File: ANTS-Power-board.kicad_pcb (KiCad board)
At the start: 2 copper layers, 90 x 90 mm, 6 parts, among them U1 TPS62916RPYR, U2 LP2985-3.3

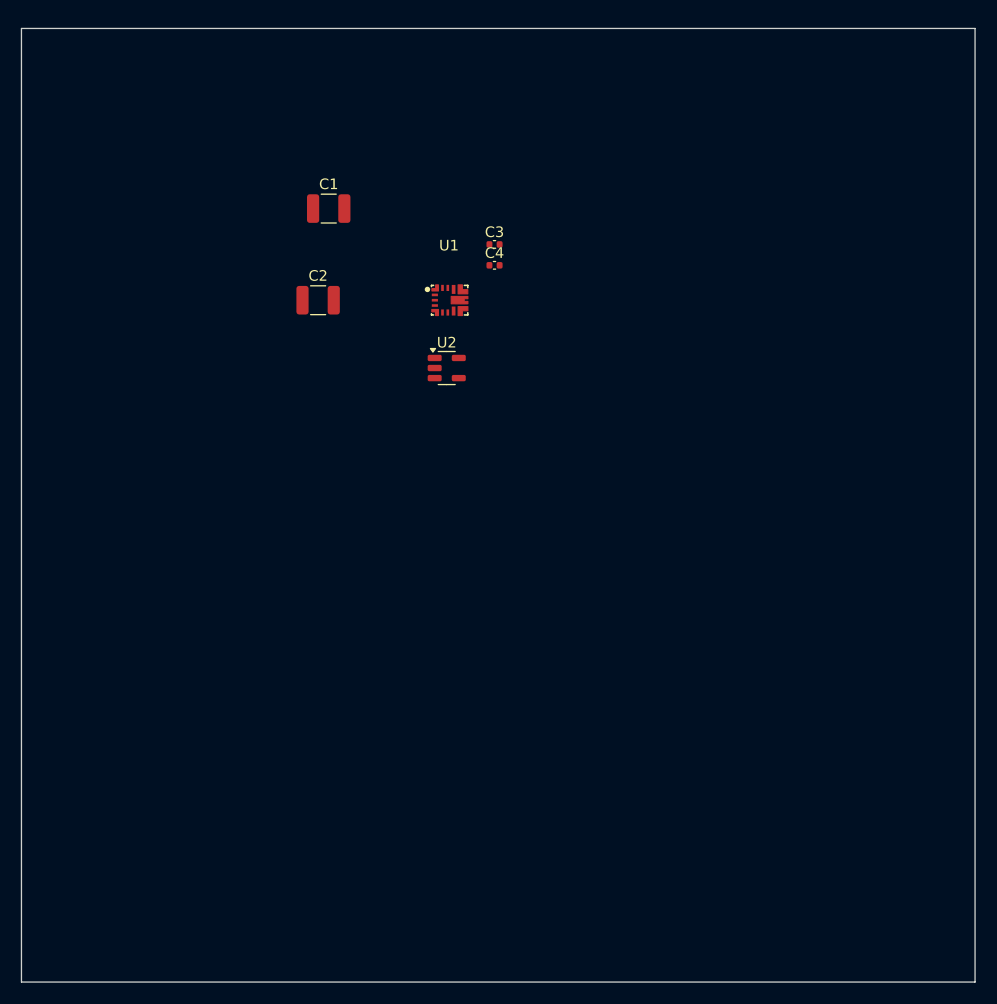
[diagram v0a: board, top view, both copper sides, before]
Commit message: Schematic finished; PCB ready for basic layout
Finished the ferrite bead footprint and setup the schematic for the PCB. Schematic has been portered over to the PCB Editor and is ready to start the basic parts layout. The PCB board is set up for the most part there are still some things to set up, but that's for later.
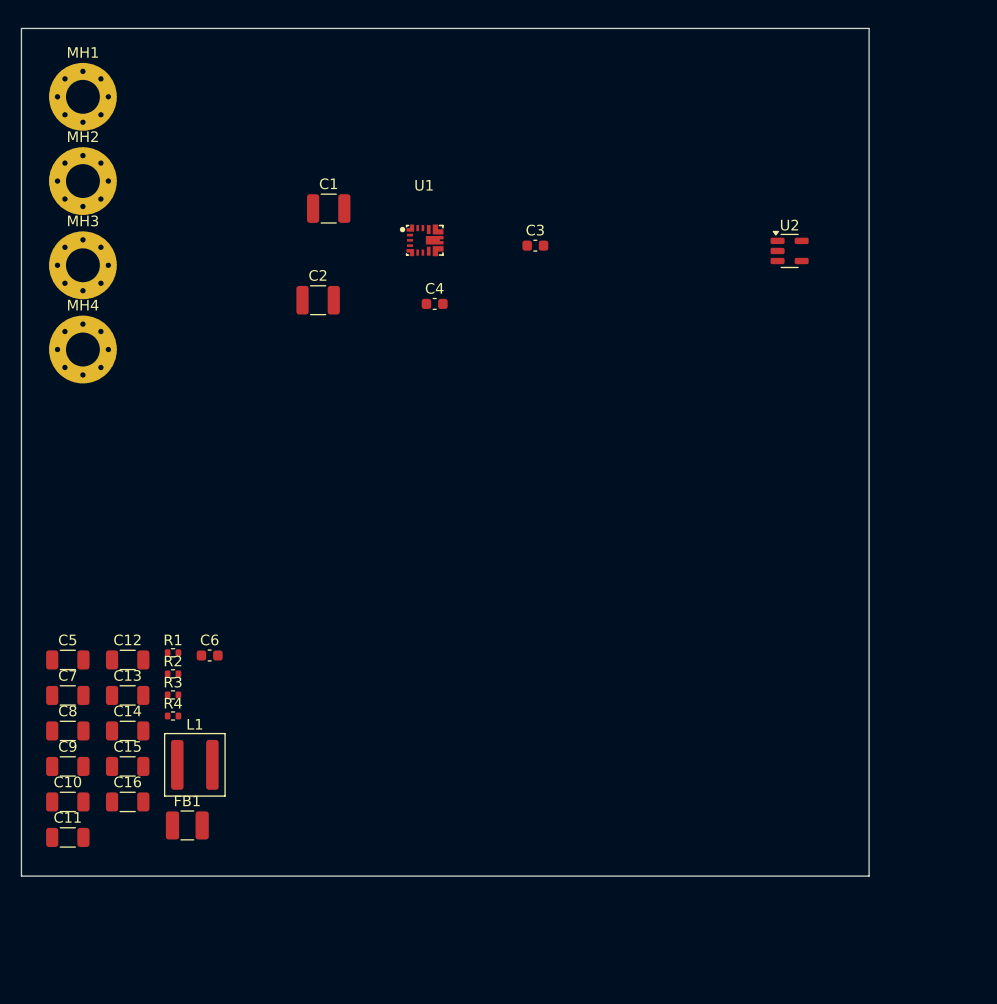
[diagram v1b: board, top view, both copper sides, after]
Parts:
- added C10: 22uF, Capacitor_SMD:C_1206_3216Metric, F.Cu at (104.4, 143.0)
- added C11: 22uF, Capacitor_SMD:C_1206_3216Metric, F.Cu at (104.4, 146.3)
- added C12: 22uF, Capacitor_SMD:C_1206_3216Metric, F.Cu at (110.0, 129.6)
- added C13: 22uF, Capacitor_SMD:C_1206_3216Metric, F.Cu at (110.0, 132.9)
- added C14: 22uF, Capacitor_SMD:C_1206_3216Metric, F.Cu at (110.0, 136.3)
- added C15: 22uF, Capacitor_SMD:C_1206_3216Metric, F.Cu at (110.0, 139.7)
- added C16: 22uF, Capacitor_SMD:C_1206_3216Metric, F.Cu at (110.0, 143.0)
- added C5: 100nF, Capacitor_SMD:C_1206_3216Metric, F.Cu at (104.4, 129.6)
- added C6: 470nF, Capacitor_SMD:C_0603_1608Metric, F.Cu at (117.8, 129.2)
- added C7: 22uF, Capacitor_SMD:C_1206_3216Metric, F.Cu at (104.4, 132.9)
- added C8: 22uF, Capacitor_SMD:C_1206_3216Metric, F.Cu at (104.4, 136.3)
- added C9: 22uF, Capacitor_SMD:C_1206_3216Metric, F.Cu at (104.4, 139.7)
- added FB1: FerriteBead, Inductor_SMD:L_1210_3225Metric, F.Cu at (115.7, 145.2)
- added L1: 1uH, Inductor_SMD:L_Coilcraft_XAL5030-XXX, F.Cu at (116.4, 139.5)
- added MH1: M3, MountingHole:MountingHole_3.2mm_M3_Pad_Via, F.Cu at (105.8, 76.5)
- added MH2: M3, MountingHole:MountingHole_3.2mm_M3_Pad_Via, F.Cu at (105.8, 84.4)
- added MH3: M3, MountingHole:MountingHole_3.2mm_M3_Pad_Via, F.Cu at (105.8, 92.4)
- added MH4: M3, MountingHole:MountingHole_3.2mm_M3_Pad_Via, F.Cu at (105.8, 100.3)
- added R1: 18.2k, Resistor_SMD:R_0402_1005Metric, F.Cu at (114.3, 128.9)
- added R2: 10k, Resistor_SMD:R_0402_1005Metric, F.Cu at (114.3, 130.9)
- added R3: 25.5k, Resistor_SMD:R_0402_1005Metric, F.Cu at (114.3, 132.9)
- added R4: 4.87k, Resistor_SMD:R_0402_1005Metric, F.Cu at (114.3, 134.9)
- C3, C4: footprint Capacitor_SMD:C_0402_1005Metric -> Capacitor_SMD:C_0603_1608Metric
- moved U2 34.2 mm to (172.5, 91.0)
- moved C4 6.72 mm to (139.0, 96.0)
- moved U1 6.12 mm to (138.0, 90.0)
- moved C3 3.85 mm to (148.5, 90.5)
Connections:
- net Net-(C5-Pad1) renamed /5V SMPS/SW
- U1 pad 14: Net-(U1-BOOT) -> /5V SMPS/BOOT
- U1 pad 2: Net-(U1-NR/SS) -> /5V SMPS/NR/SS
- U1 pad 3: Net-(U1-FB) -> /5V SMPS/FB
- U1 pad 4: Net-(U1-VO) -> /5V SMPS/VO
- U1 pad 5: Net-(U1-PG) -> /5V SMPS/PG
- U1 pad 6: Net-(U1-S-CONF) -> /5V SMPS/S-CONF
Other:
- board size 90 x 90 mm -> 80 x 80 mm
- rule pad_to_mask_clearance: 0 -> 0.1

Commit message: Wiring done; grounding and error checking still needs to be done
Wiring done; everything still needs to be grounded, error checking, labeling on the board, and final stuff like that still need to be done
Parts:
- moved MH4 83.1 mm to (175.5, 145.5)
- moved C16 77.3 mm to (166.7, 90.3), turned to 90 degrees
- moved C15 73.2 mm to (164.2, 90.3), turned to 90 degrees
- moved MH2 70.4 mm to (175.5, 74.5)
- moved FB1 68.1 mm to (157.8, 91.8), turned to 180 degrees
- moved C11 64.9 mm to (134.0, 88.6), turned to 90 degrees
- moved U2 60.4 mm to (136.5, 139.5)
- moved C9 57.8 mm to (131.5, 88.6), turned to 90 degrees
- moved C10 54.9 mm to (131.4, 95.2), turned to -90 degrees
- moved MH3 53.2 mm to (104.5, 145.5)
- moved C13 51.7 mm to (136.5, 88.6), turned to 90 degrees
- moved C7 50.7 mm to (129.0, 88.6), turned to 90 degrees
- moved C14 48.9 mm to (136.4, 95.2), turned to -90 degrees
- moved L1 48.1 mm to (122.9, 91.8), turned to 180 degrees
- moved C8 47.9 mm to (128.9, 95.2), turned to -90 degrees
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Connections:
- C10 pad 1: /5V SMPS/VO -> 5V_out
- C11 pad 1: /5V SMPS/VO -> 5V_out
- C12 pad 1: /5V SMPS/VO -> 5V_out
- C13 pad 1: /5V SMPS/VO -> 5V_out
- C14 pad 1: /5V SMPS/VO -> 5V_out
- C7 pad 1: /5V SMPS/VO -> 5V_out
- C8 pad 1: /5V SMPS/VO -> 5V_out
- C9 pad 1: /5V SMPS/VO -> 5V_out
- FB1 pad 2: /5V SMPS/VO -> 5V_out
- L1 pad 1: /5V SMPS/VO -> 5V_out
- R2 pad 1: /5V SMPS/VO -> 5V_out
- R3 pad 1: /5V SMPS/VO -> 5V_out
- U1 pad 4: /5V SMPS/VO -> 5V_out
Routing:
- net 5V_out: track 0.00 -> 192.7 mm
- net VBAT+: track 0.00 -> 32.3 mm
- net /5V SMPS/SW: track 0.00 -> 9.90 mm
- net /5V SMPS/BOOT: track 0.00 -> 5.52 mm
- net /5V SMPS/FB: track 0.00 -> 3.90 mm
- net /5V SMPS/NR/SS: track 0.00 -> 2.65 mm
- net /5V SMPS/PG: track 0.00 -> 1.99 mm
- net /5V SMPS/S-CONF: track 0.00 -> 1.09 mm
- net VBAT-: vias 0 -> 51
- added copper zone on B.Cu, net VBAT-

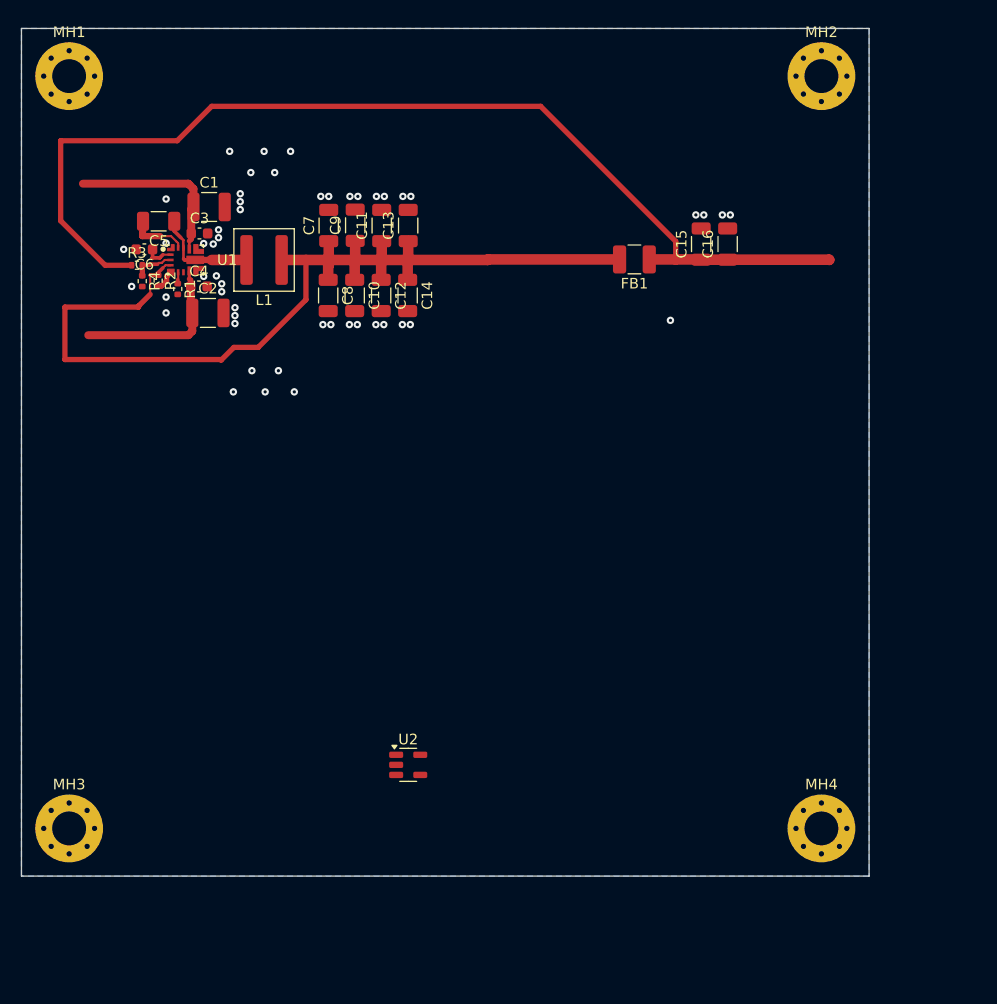
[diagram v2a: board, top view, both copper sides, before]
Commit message: Add connectors & adjust board cuts
- Add DF11 and ScrewTerminals
- Add new edge cuts
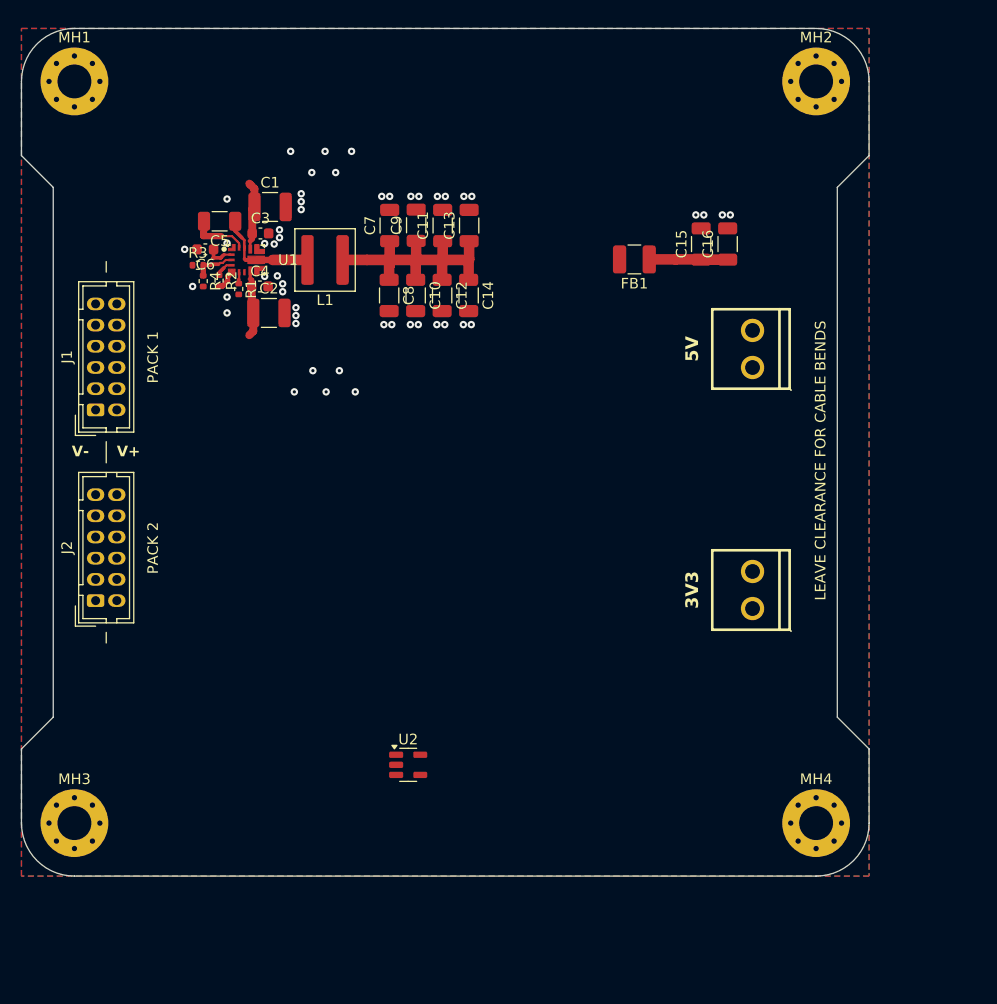
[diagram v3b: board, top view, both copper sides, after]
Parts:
- added J1: DF11-12DP, Connector_Hirose:Hirose_DF11-12DP-2DSA_2x06_P2.00mm_Vertical, F.Cu at (107.0, 106.0)
- added J2: DF11-12DP, Connector_Hirose:Hirose_DF11-12DP-2DSA_2x06_P2.00mm_Vertical, F.Cu at (107.0, 124.0)
- added J3: Phoenix 1751248, ScrewTerminal:CONN-TH_MKDS1-2-3.5, F.Cu at (169.0, 100.2)
- added J4: Phoenix 1751248, ScrewTerminal:CONN-TH_MKDS1-2-3.5, F.Cu at (169.0, 123.0)
- moved C10 5.76 mm to (137.2, 95.2)
- moved C12 5.76 mm to (139.7, 95.2)
- moved C14 5.76 mm to (142.2, 95.2)
- moved C8 5.76 mm to (134.7, 95.2)
- moved C1 5.76 mm to (123.5, 86.8)
- moved C2 5.76 mm to (123.4, 96.8)
- moved C3 5.76 mm to (122.6, 89.3)
- moved C6 5.76 mm to (117.4, 90.8)
- moved C11 5.75 mm to (139.8, 88.6)
- moved C13 5.75 mm to (142.3, 88.6)
- moved C4 5.75 mm to (122.5, 94.3)
- moved C5 5.75 mm to (118.7, 88.2)
- moved C7 5.75 mm to (134.8, 88.6)
- moved C9 5.75 mm to (137.3, 88.6)
- moved L1 5.75 mm to (128.7, 91.8)
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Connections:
- C10 pad 1: 5V_out -> /5V SMPS/VO
- C11 pad 1: 5V_out -> /5V SMPS/VO
- C12 pad 1: 5V_out -> /5V SMPS/VO
- C13 pad 1: 5V_out -> /5V SMPS/VO
- C14 pad 1: 5V_out -> /5V SMPS/VO
- C15 pad 1: 5V_out -> 5V_OUTPUT
- C16 pad 1: 5V_out -> 5V_OUTPUT
- C7 pad 1: 5V_out -> /5V SMPS/VO
- C8 pad 1: 5V_out -> /5V SMPS/VO
- C9 pad 1: 5V_out -> /5V SMPS/VO
- FB1 pad 1: 5V_out -> 5V_OUTPUT
- FB1 pad 2: 5V_out -> /5V SMPS/VO
- L1 pad 1: 5V_out -> /5V SMPS/VO
- R2 pad 1: 5V_out -> /5V SMPS/VO
- R3 pad 1: 5V_out -> 5V_OUTPUT
- U1 pad 4: 5V_out -> /5V SMPS/VO
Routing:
- net 5V_out: track 192.7 -> 0.00 mm
- net /5V SMPS/VO: track 0.00 -> 28.3 mm
- net VBAT+: track 32.3 -> 12.9 mm
- net 5V_OUTPUT: track 0.00 -> 7.41 mm
- net VBAT-: vias 51 -> 50
- added copper zone on F.Cu, net VBAT-
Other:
- outline, holes or cut-outs redrawn
- board text added: "3V3"
- board text added: "5V"
- board text added: "LEAVE CLEARANCE FOR CABLE BENDS"
- board text added: "PACK 1"
- board text added: "PACK 2"
- board text added: "V+"
- board text added: "V-"

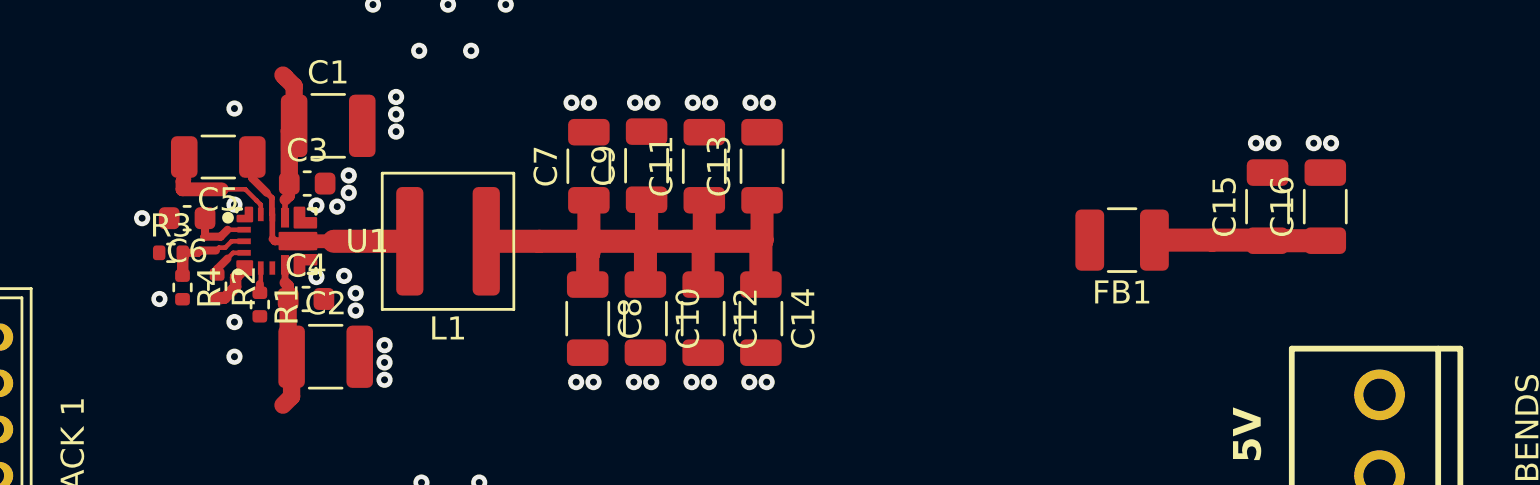
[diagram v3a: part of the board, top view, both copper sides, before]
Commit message: Made some fill zones
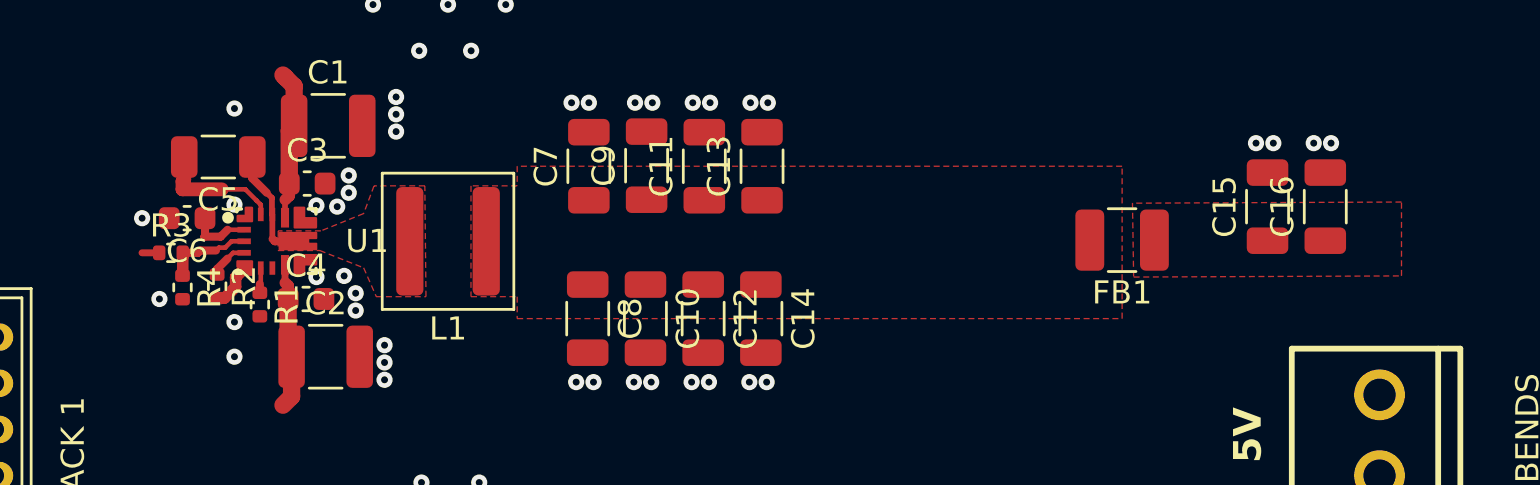
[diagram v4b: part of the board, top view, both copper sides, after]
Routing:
- net /5V SMPS/VO: track 28.3 -> 1.71 mm
- net 5V_OUTPUT: track 7.41 -> 0.78 mm
- net /5V SMPS/SW: track 9.90 -> 5.05 mm
- added copper zone on F.Cu, net /5V SMPS/SW
- added copper zone on F.Cu, net /5V SMPS/VO
- added copper zone on F.Cu, net 5V_OUTPUT

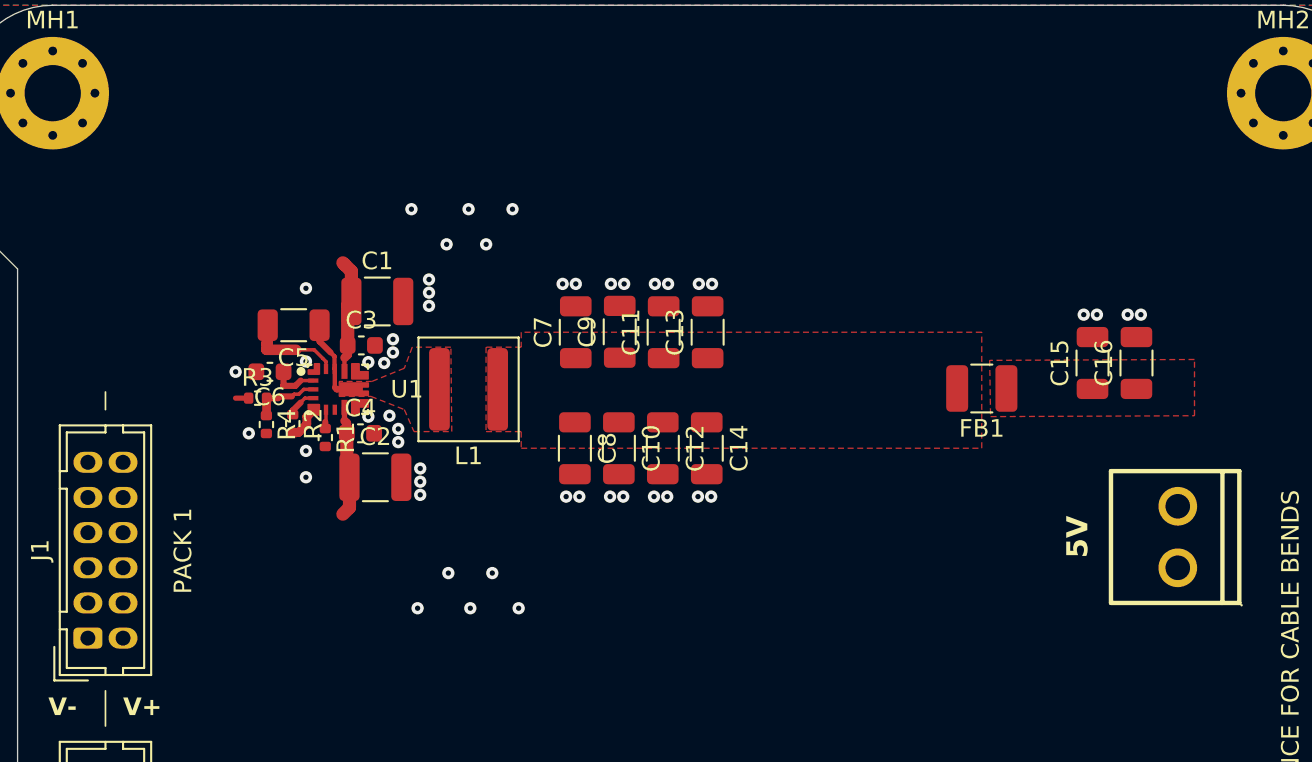
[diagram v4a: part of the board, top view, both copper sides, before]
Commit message: Did the changes that Tri asked
Did the changes that Tri asked
Labeling on board and some fixes on rule checker needed to be done.
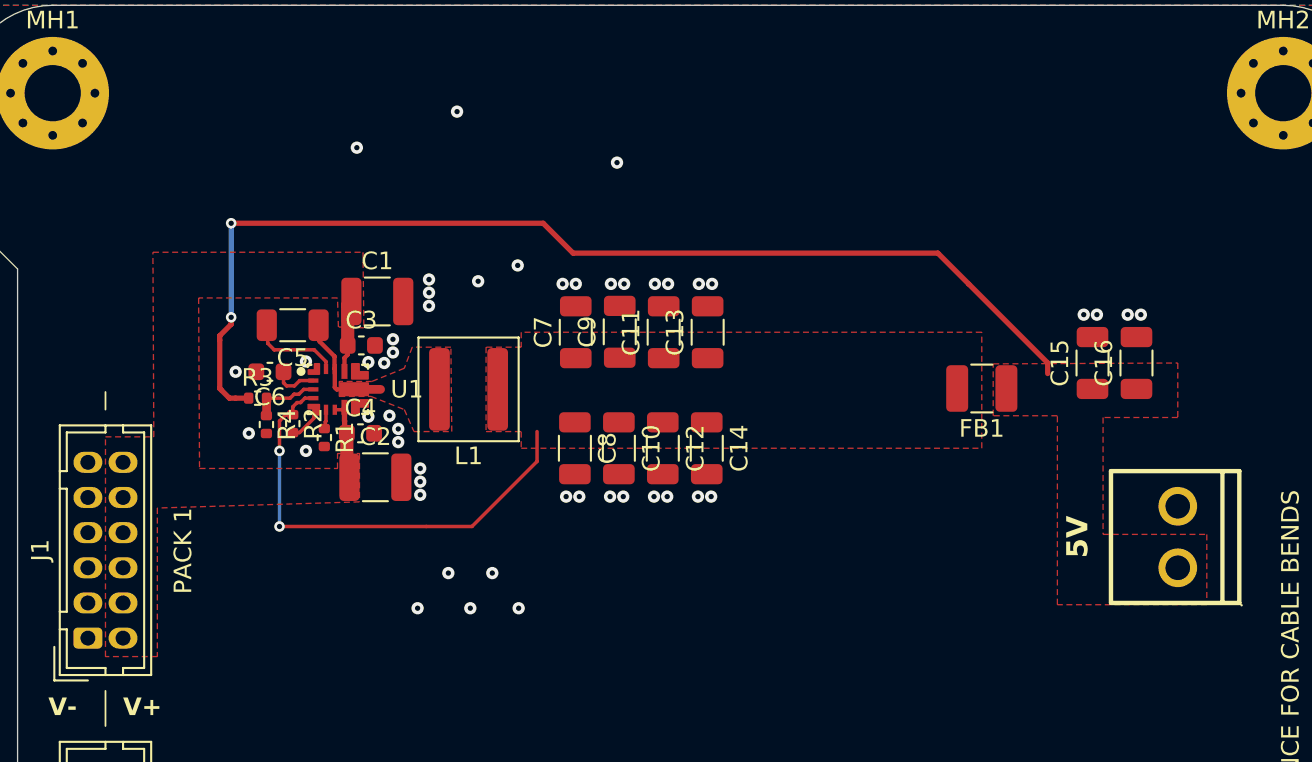
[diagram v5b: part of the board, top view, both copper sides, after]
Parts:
- moved C5 0.05 mm to (118.7, 88.2)
- moved R1 0.05 mm to (120.5, 94.6)
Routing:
- net 5V_OUTPUT: track 0.78 -> 61.9 mm, vias 0 -> 2
- net /5V SMPS/VO: track 1.71 -> 26.6 mm, vias 0 -> 2
- net VBAT+: track 12.9 -> 8.85 mm
- net /5V SMPS/SW: track 5.05 -> 6.55 mm
- net VBAT-: vias 50 -> 48
- added copper zone on F.Cu, net VBAT+
